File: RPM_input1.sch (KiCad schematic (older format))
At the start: 30 parts, among them P43 CONN_1, P44 CONN_1, P45 CONN_1, P46 CONN_1, P47 CONN_1, SW8 SWITCH_INV, U8 TL082CN, U9 LM1815

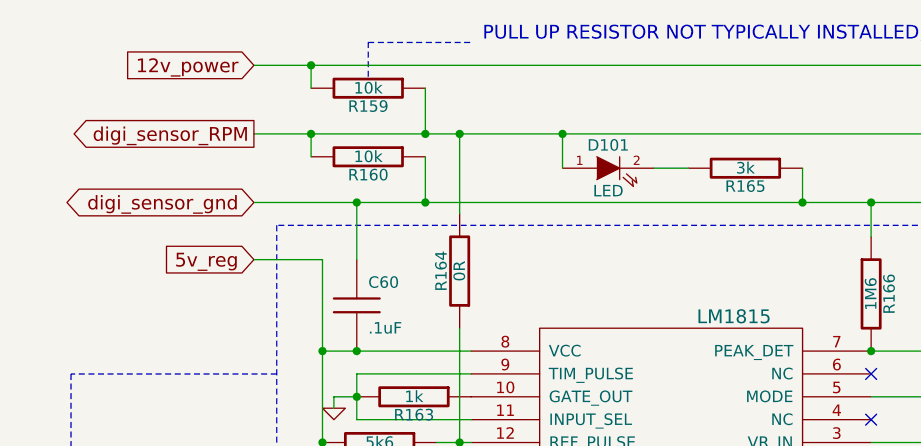
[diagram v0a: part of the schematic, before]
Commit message: DFH mans up a bit. Perhaps usable for something at this point, like making trips to the local store ;)
I connected TA pins to sub circuits, fixed a number if items discussed in the DIYEFI forums. This is it's 21st version, so it was time for it to man up a bit, and become something potentially useful.

Signed-off-by: Jared Harvey <TortiseGIT@jaredharvey.com>
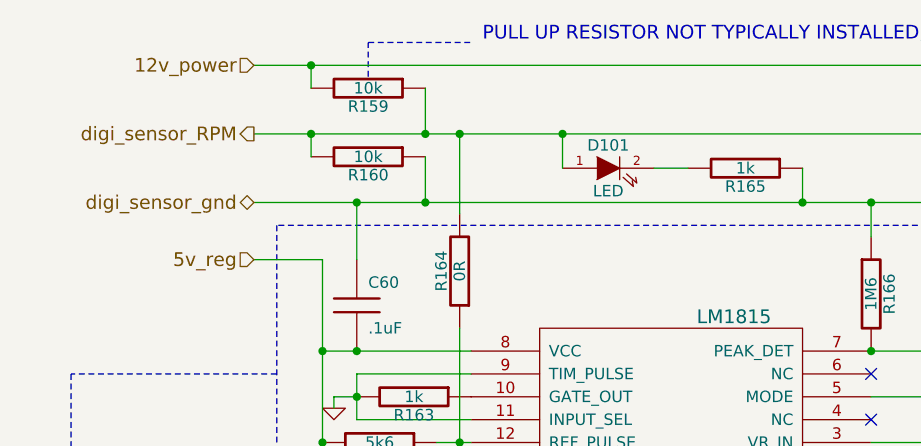
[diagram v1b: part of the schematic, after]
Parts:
- C60: Field10 (none) -> multilayer ceramic; Field11 (none) -> other,more,stuff; Field4 (none) -> newark,97M4164; Field5 (none) -> vendor1, smd w hem; Field6 (none) -> vendor2, thru w hem; Field7 (none) -> vendor2, smd w hem; Field8 (none) -> 50,V; Field9 (none) -> 20,%
- C61: Field10 (none) -> multilayer ceramic; Field11 (none) -> other,more,stuff; Field4 (none) -> newark,93K3279; Field5 (none) -> vendor1, smd w hem; Field6 (none) -> vendor2, thru w hem; Field7 (none) -> vendor2, smd w hem; Field8 (none) -> 100,V; Field9 (none) -> 10,%
- C62: Field10 (none) -> multilayered ceramic; Field11 (none) -> other,more,stuff; Field4 (none) -> newark,36K5919; Field5 (none) -> vendor1, smd w hem; Field6 (none) -> vendor2, thru w hem; Field7 (none) -> vendor2, smd w hem; Field8 (none) -> 100,V; Field9 (none) -> 5,%
- C63: Field10 (none) -> multilayer ceramic; Field11 (none) -> other,more,stuff; Field4 (none) -> newark,89F3212; Field5 (none) -> vendor1, smd w hem; Field6 (none) -> vendor2, thru w hem; Field7 (none) -> vendor2, smd w hem; Field8 (none) -> 50,V; Field9 (none) -> 20,%
- C64: Field10 (none) -> multilayer ceramic; Field11 (none) -> other,more,stuff; Field4 (none) -> newark,97M4158; Field5 (none) -> vendor1, smd w hem; Field6 (none) -> vendor2, thru w hem; Field7 (none) -> vendor2, smd w hem; Field8 (none) -> 10,V; Field9 (none) -> 10,%
- D101: A (none) -> 10mA; V (none) -> 12V; construct (none) -> LED with resistor included; misc (none) -> other,more,stuff; vend1,smd e hem (none) -> newark,; vend2, smd w hem (none) -> digi,; vend2, thru w hem (none) -> digi,; vendor1, thru e hem (none) -> newark,58K2517
- R159, R160: Field10 (none) -> carbon film; Field11 (none) -> other,more,stuff; Field4 (none) -> newark,38k0328; Field5 (none) -> vendor1, smd w hem; Field6 (none) -> vendor2, thru w hem; Field7 (none) -> vendor2, smd w hem; Field8 (none) -> 250,mW; Field9 (none) -> 5,%
- R161, R168: Field10 (none) -> carbon film; Field11 (none) -> other,more,stuff; Field4 (none) -> newark,38K0382; Field5 (none) -> vendor1, smd w hem; Field6 (none) -> vendor2, thru w hem; Field7 (none) -> vendor2, smd w hem; Field8 (none) -> 250,mW; Field9 (none) -> 5,%
- R162: Field10 (none) -> carbon film; Field11 (none) -> other,more,stuff; Field4 (none) -> newark,58K4949; Field5 (none) -> vendor1, smd w hem; Field6 (none) -> vendor2, thru w hem; Field7 (none) -> vendor2, smd w hem; Field8 (none) -> 500,mW; Field9 (none) -> 5,%
- R163: W (none) -> 1/4w; construct (none) -> carbon film; misc (none) -> other,more,stuff; tol (none) -> 5%; vend1,smd e hem (none) -> newark,52K9725; vend2, smd w hem (none) -> digi,CRCW08051K00JNEA; vend2, thru w hem (none) -> digi,OD102J-ND; vendor1, thru e hem (none) -> newark,65K2365
- R164: TOL (none) -> 5%; W (none) -> 1/4W; construct (none) -> carbon film; misc (none) -> other,more,stuff; vend1,smd e hem (none) -> newark,36C9353; vend2, smd w hem (none) -> digi,CRCW08050000ZSTA-ND; vend2, thru w hem (none) -> digi,604HR025E-ND; vendor1, thru e hem (none) -> newark,64K9335
- R165: value 3k -> 1k; W (none) -> 1/4w; construct (none) -> carbon film; misc (none) -> other,more,stuff; tol (none) -> 5%; vend1,smd e hem (none) -> newark,52K9725; vend2, smd w hem (none) -> digi,CRCW08051K00JNEA; vend2, thru w hem (none) -> digi,OD102J-ND; vendor1, thru e hem (none) -> newark,65K2365
- R166: Field10 (none) -> carbon composition; Field11 (none) -> other,more,stuff; Field4 (none) -> newark,73K0277; Field5 (none) -> vendor1, smd w hem; Field6 (none) -> vendor2, thru w hem; Field7 (none) -> vendor2, smd w hem; Field8 (none) -> 250,mW; Field9 (none) -> 5,%
- R167: Field10 (none) -> carbon film; Field11 (none) -> other,more,stuff; Field4 (none) -> newark,58K5022; Field5 (none) -> vendor1, smd w hem; Field6 (none) -> vendor2, thru w hem; Field7 (none) -> vendor2, smd w hem; Field8 (none) -> 250,mW; Field9 (none) -> 5,%
- R169: Field10 (none) -> metal film; Field11 (none) -> other,more,stuff; Field4 (none) -> newark,58K3858; Field5 (none) -> vendor1, smd w hem; Field6 (none) -> vendor2, thru w hem; Field7 (none) -> vendor2, smd w hem; Field8 (none) -> 250,mW; Field9 (none) -> 1,%
- R170: Field10 (none) -> metal film; Field11 (none) -> other,more,stuff; Field4 (none) -> newark,94C4880; Field5 (none) -> vendor1, smd w hem; Field6 (none) -> vendor2, thru w hem; Field7 (none) -> vendor2, smd w hem; Field8 (none) -> 400,mW; Field9 (none) -> 1,%
- R171: Field10 (none) -> metal film; Field11 (none) -> other,more,stuff; Field4 (none) -> newark,71M1054; Field5 (none) -> vendor1, smd w hem; Field6 (none) -> vendor2, thru w hem; Field7 (none) -> vendor2, smd w hem; Field8 (none) -> 500,mW; Field9 (none) -> 1,%
- R172: Field10 (none) -> metal film; Field11 (none) -> other,more,stuff; Field4 (none) -> newark,58K3819; Field5 (none) -> vendor1, smd w hem; Field6 (none) -> vendor2, thru w hem; Field7 (none) -> vendor2, smd w hem; Field8 (none) -> 250,mW; Field9 (none) -> 1,%
- R173: Field10 (none) -> metal film; Field11 (none) -> other,more,stuff; Field4 (none) -> newark,58K3844; Field5 (none) -> vendor1, smd w hem; Field6 (none) -> vendor2, thru w hem; Field7 (none) -> vendor2, smd w hem; Field8 (none) -> 250,mW; Field9 (none) -> 1,%
- R174: Field10 (none) -> metal film; Field11 (none) -> other,more,stuff; Field4 (none) -> newark,58K3797; Field5 (none) -> vendor1, smd w hem; Field6 (none) -> vendor2, thru w hem; Field7 (none) -> vendor2, smd w hem; Field8 (none) -> 250,mW; Field9 (none) -> 1,%
- SW8: Field10 (none) -> x,x; Field11 (none) -> x,x,x; Field4 (none) -> vendor1, thru w hem; Field5 (none) -> vendor1, thru smd w hem; Field6 (none) -> vendor2, thru w hem; Field7 (none) -> vendor2, thru smd w hem; Field8 (none) -> x,x; Field9 (none) -> x,x
- U8: Field10 (none) -> opamp; Field11 (none) -> other,more,stuff; Field4 (none) -> newark,89K1104; Field5 (none) -> vendor1, smd w hem; Field6 (none) -> digi,497-2213-5-ND; Field7 (none) -> vendor2, smd w hem; Field8 (none) -> x,x; Field9 (none) -> x,x
- U9: Field10 (none) -> VR RPM chip; Field11 (none) -> x,x,x; Field4 (none) -> newark,41K3517; Field5 (none) -> vendor2, thru e hem; Field6 (none) -> vendor2, thru w hem; Field7 (none) -> newark,41k3517; Field8 (none) -> x,x; Field9 (none) -> x,x

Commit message: Changed from LM chip, to JBPerf VR board.
Signed-off-by: Jared Harvey <TortiseGIT@jaredharvey.com>
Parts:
- removed C61: .001uF, C1V7, symbol C
- removed C62: 330pF, C1V7, symbol C
- removed C63: .33uF, C1V7, symbol C
- removed R166: 1M6, R4-SM0805, symbol R
- removed R167: 18k, R4-SM0805, symbol R
- removed R168: 5k, R4-SM0805, symbol R
- removed SW8: SWITCH_INV, SIL-3, symbol SWITCH_INV
- removed U9: LM1815, SO14E, symbol LM1815
- added P38, P39: CONN_1, 1PIN, symbol CONN_1
- added U361: VR_JBPERF, VR_JBPERF, symbol VR_JBPERF
- R161: value 5k6 -> 1k
- R162: value 150k -> 5k
- R163: value 1k -> 5k
- R164: value 0R -> 1k
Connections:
- net labels added: digi_sensor_RPM1, digi_sensor_RPM2
- net labels removed: digi_sensor_RPM
- wire segments 59 -> 56
- no-connect marks 4 -> 0
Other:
- note added: "HALL FILTER CIRCUIT"
- note added: "OPTIONAL 5K TO WEAKEN STRONG SIGNALS.\nOPTIONAL 1K PULL TO ALLOW HALL TO PULL DOWN"
- note added: "VR CIRCUIT OR HALL"
- note removed: "HALL SENSOR CIRCUIT"
- note removed: "RECOMMENDED TO REMOVE 150K AND SHORT CAP TO CREATE SQUARE WAVE OUTPUT, NOT TIMMED PULSE"
- note removed: "SWITCHING THIS WILL CHANGE THE MODE OF OUTPUT SIGNAL FOR THE VR CIRCUIT"
- note removed: "TO SWITCH THESE, THERE WILL BE THREE PADS AND YOU WILL JUMPER 2 FOR YOUR NEEDS"
- note removed: "VR CIRCUIT"
- moved on the sheet: C60, P43, P44, R161, R162, R163, R164
